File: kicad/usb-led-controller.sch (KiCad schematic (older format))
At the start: 42 parts, among them J1 SWD, J2 PWR, J3 USB, J4 PWM_0, J5 PWM_1, J6 WS2812_0, J7 WS2812_1, Q1 NVS4409N, Q2 NVS4409N, Q3 NVS4409N, Q4 NVS4409N, Q5 NVS4409N, Q6 NVS4409N, U1 SN74LV1T125, U2 SN74LV1T125, U3 STM32F042F6Px, U4 MIC5501-XYM5, U5 USBLC6, U6 SN74LVC1G04

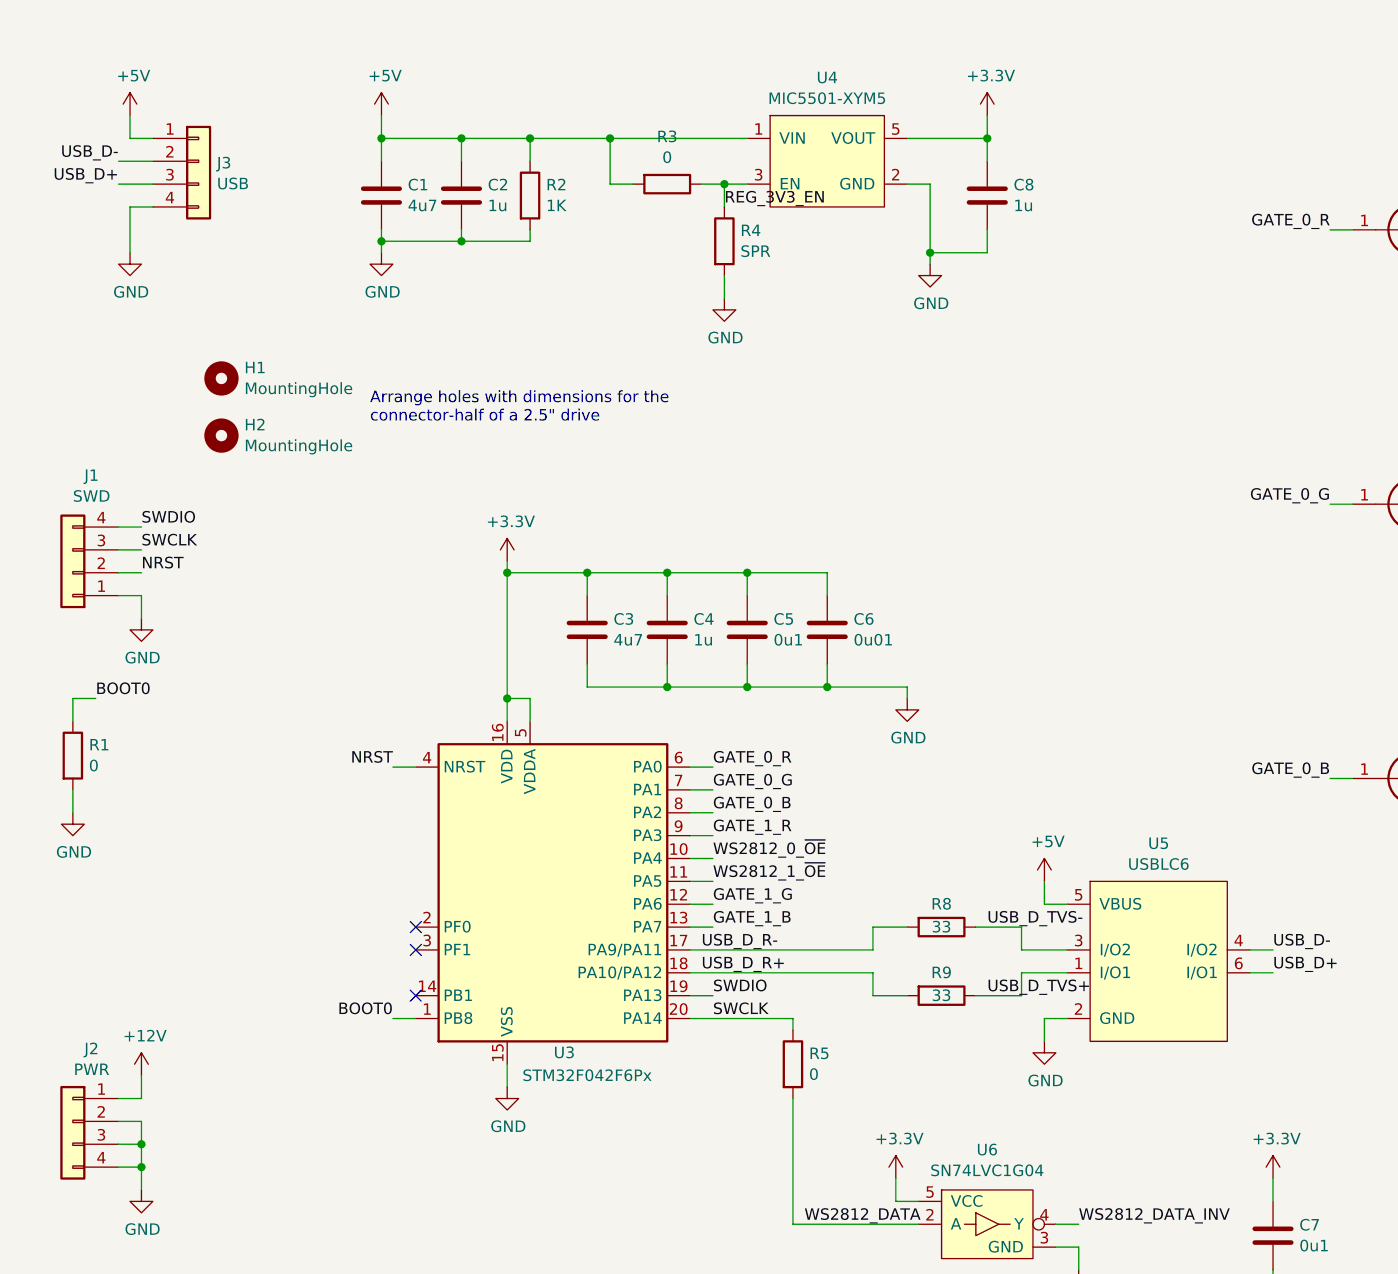
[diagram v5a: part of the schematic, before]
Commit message: Added polyfuses and reduced board size
This is much more reasonable. No need to take up all that space.
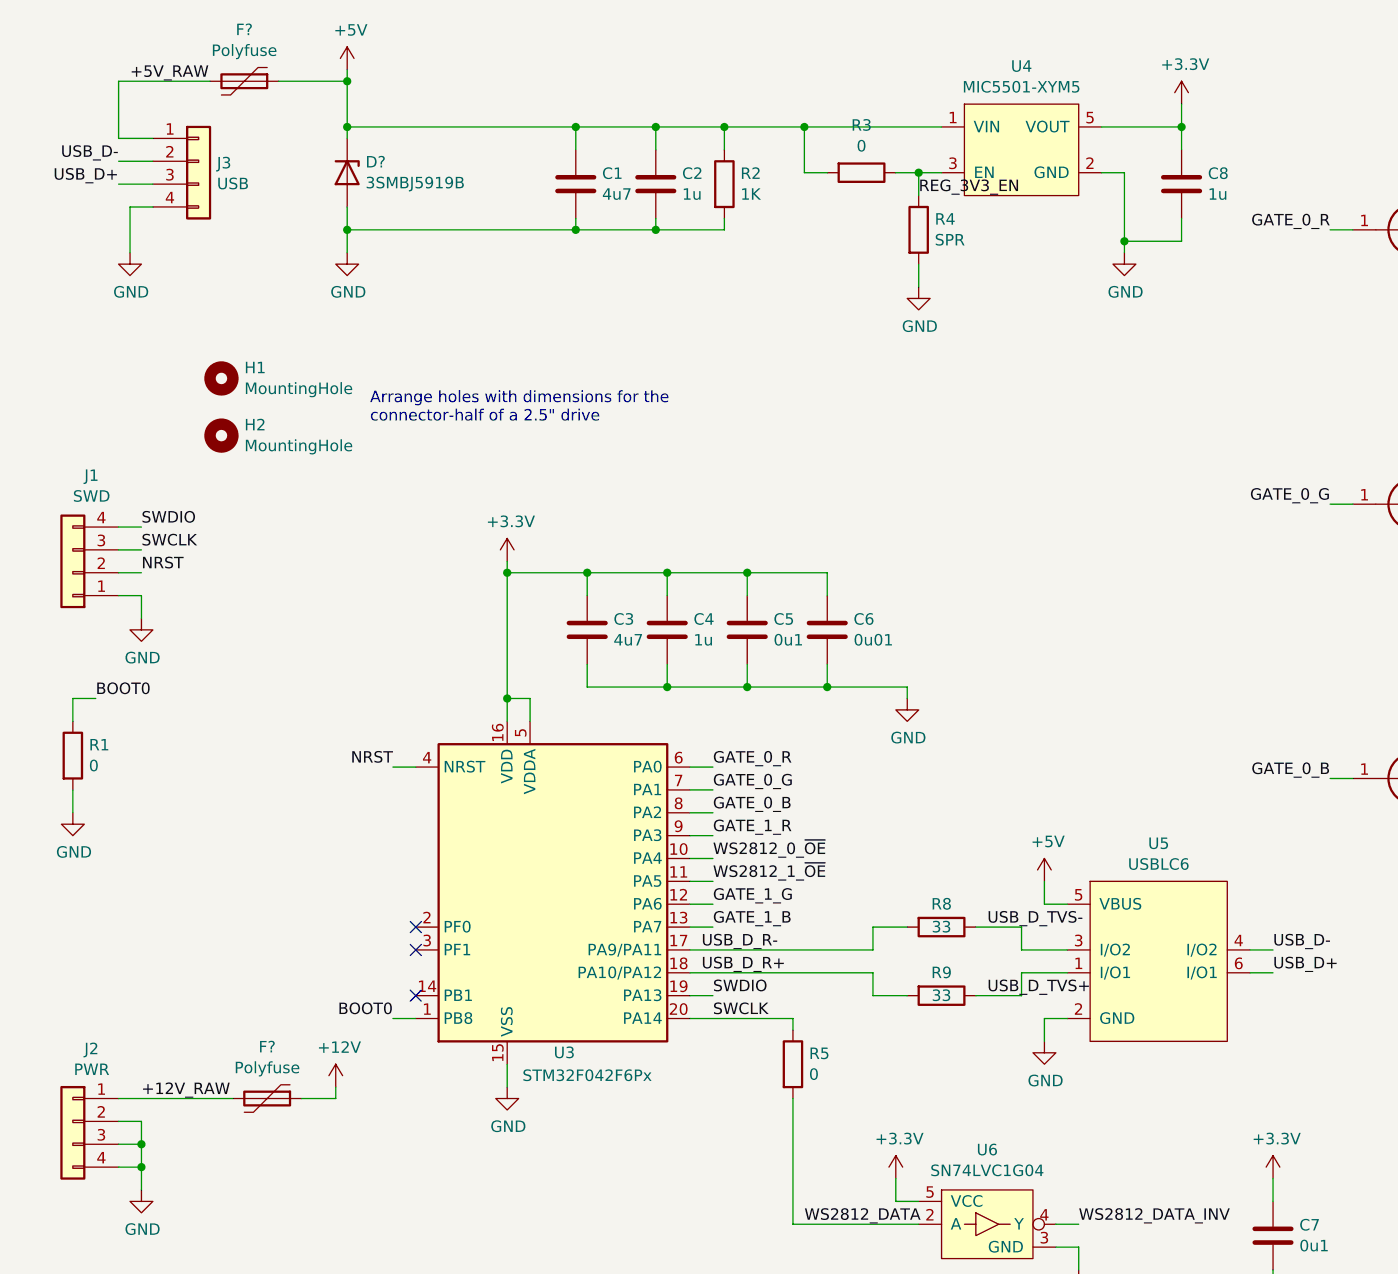
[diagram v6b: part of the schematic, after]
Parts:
- added D?: 3SMBJ5919B, Diode_SMD:D_SMB, symbol Device:D_Zener
- added F? (x2): Polyfuse, Resistor_SMD:R_1812_4532Metric, symbol Device:Polyfuse
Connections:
- net +12V: now also F?.1; no longer J2.1 (Pin_1)
- net +5V: now also D?.1 (K), F?.1; no longer J3.1 (Pin_1)
- net GND: now also D?.2 (A)
- new net +12V_RAW: F?.2, J2.1 (Pin_1)
- new net +5V_RAW: F?.2, J3.1 (Pin_1)
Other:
- moved on the sheet: C1, C2, C8, R2, R3, R4, U4

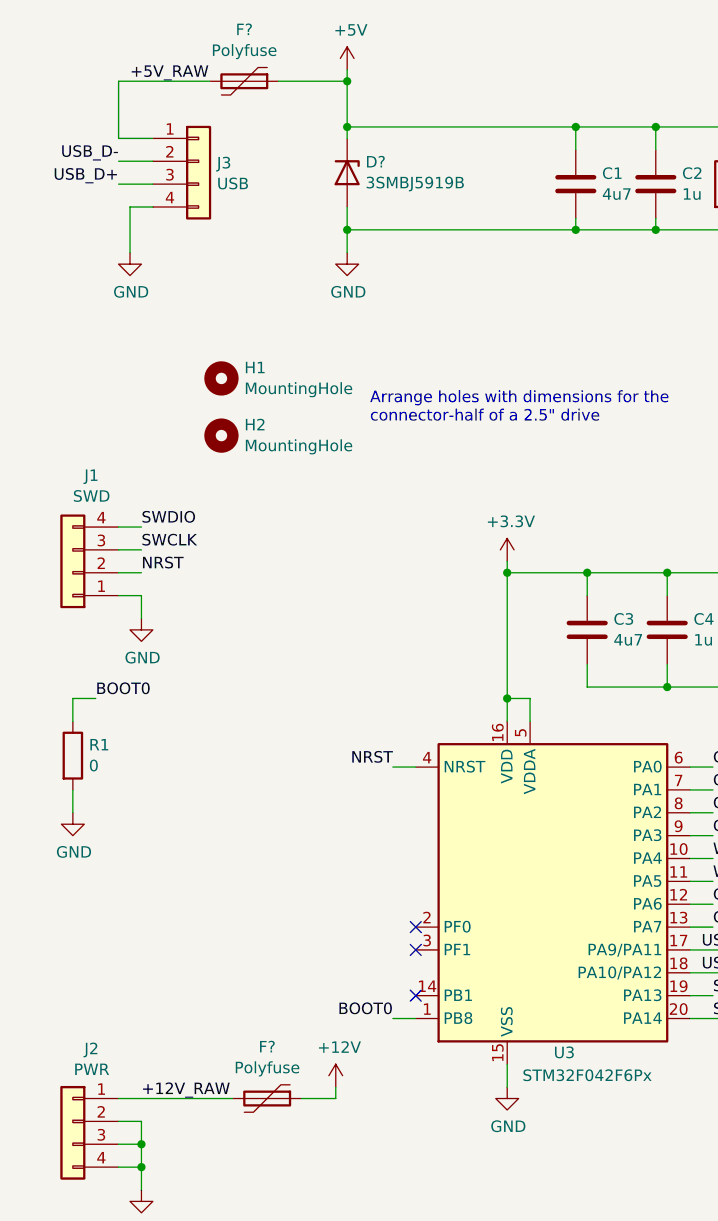
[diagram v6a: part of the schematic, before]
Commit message: Added power planes to 3rd layer
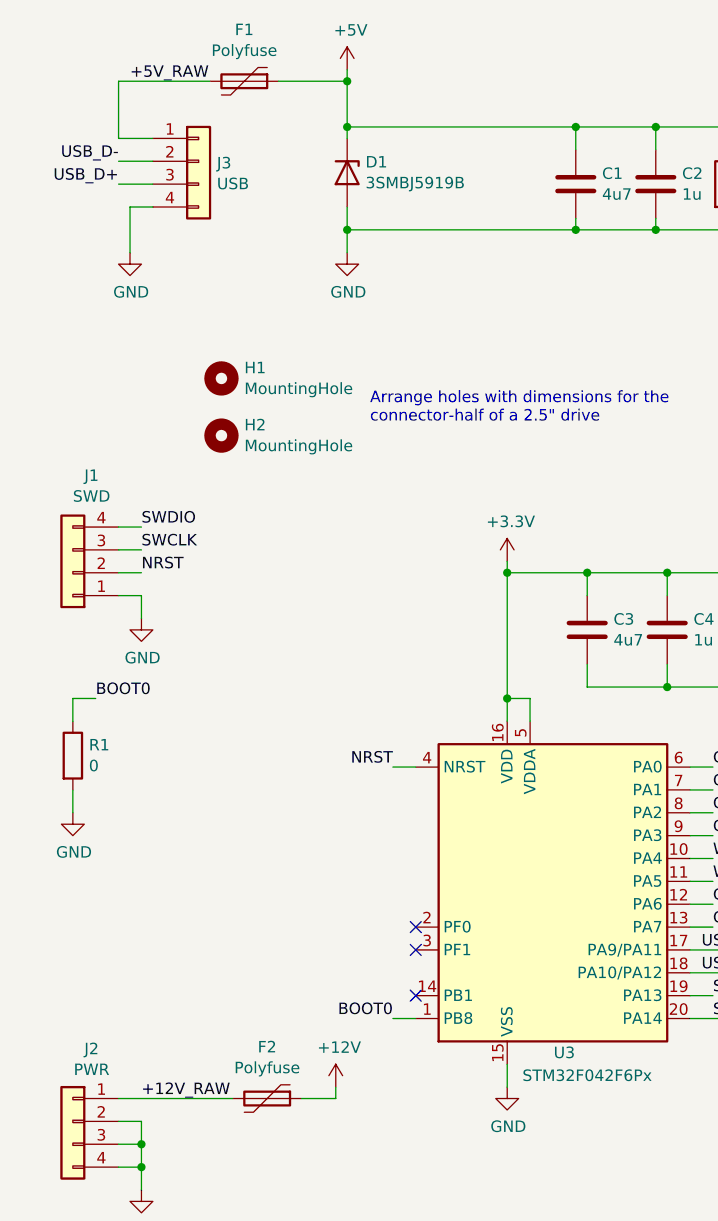
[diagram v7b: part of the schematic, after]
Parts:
- gave numbers to parts that had none: 3
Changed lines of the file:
@@
 	4050 7500 4050 6800
 $Comp
-L Device:D_Zener D?
+L Device:D_Zener D1
 U 1 1 5FDE372A
 P 2000 1150
-F 0 "D?" V 1954 1230 50  0000 L CNN
+F 0 "D1" V 1954 1230 50  0000 L CNN
 F 1 "3SMBJ5919B" V 2045 1230 50  0000 L CNN
 F 2 "Diode_SMD:D_SMB" H 2000 1150 50  0001 C CNN
@@
 	2000 1400 2000 1500
 $Comp
-L Device:Polyfuse F?
+L Device:Polyfuse F1
 U 1 1 5FE992D3
 P 1550 750
-F 0 "F?" V 1325 750 50  0000 C CNN
+F 0 "F1" V 1325 750 50  0000 C CNN
 F 1 "Polyfuse" V 1416 750 50  0000 C CNN
 F 2 "Resistor_SMD:R_1812_4532Metric" H 1600 550 50  0001 L CNN
@@
 $EndComp
 $Comp
-L Device:Polyfuse F?
+L Device:Polyfuse F2
 U 1 1 5FE9B09A
 P 1650 5200
-F 0 "F?" V 1425 5200 50  0000 C CNN
+F 0 "F2" V 1425 5200 50  0000 C CNN
 F 1 "Polyfuse" V 1516 5200 50  0000 C CNN
 F 2 "Resistor_SMD:R_1812_4532Metric" H 1700 5000 50  0001 L CNN

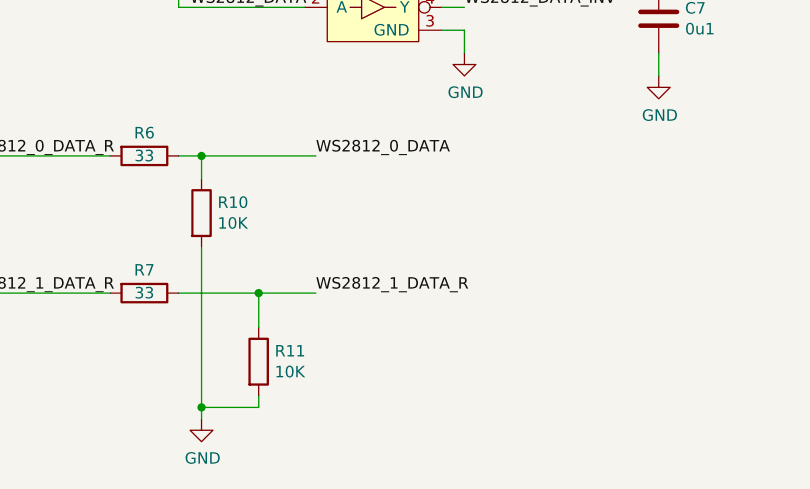
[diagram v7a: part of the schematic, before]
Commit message: Cmopleted initial routing
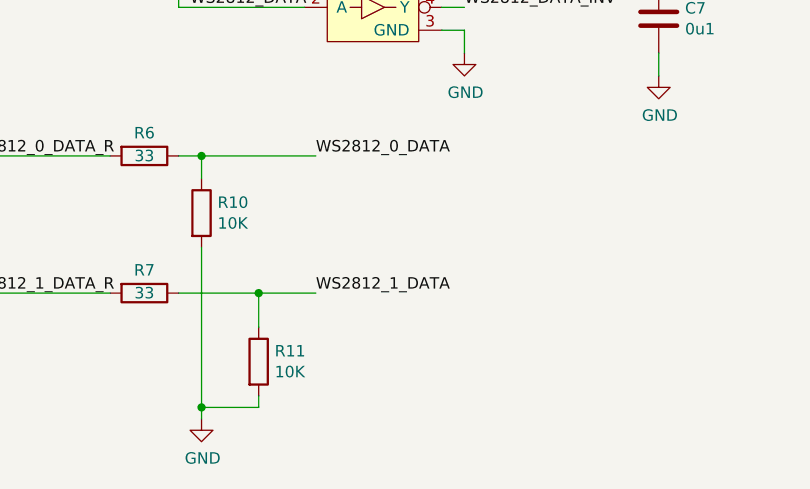
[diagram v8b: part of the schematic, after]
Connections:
- net WS2812_1_DATA: now also R11.1, R7.1
- net WS2812_1_DATA_R: no longer R11.1, R7.1
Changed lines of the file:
@@
 	4550 6400 4050 6400
 Text Label 4550 7000 0    50   ~ 0
-WS2812_1_DATA_R
+WS2812_1_DATA
 Wire Wire Line
 	4550 7000 4300 7000
